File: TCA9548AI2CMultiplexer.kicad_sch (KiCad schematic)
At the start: 13 parts, among them U2 TCA9548APWR, U3 PCF8574TS

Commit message: Initial commit.
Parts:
- removed R41: 10kΩ, Resistor_SMD:R_0805_2012Metric, symbol Device:R
- removed R41 (x2): 0Ω, Resistor_SMD:R_0805_2012Metric, symbol Device:R
- added J14: ~{RESET}, Connector_PinHeader_2.54mm:PinHeader_1x02_P2.54mm_Vertical, symbol Connector_Generic:Conn_01x02
- added R32: 10kΩ, Resistor_SMD:R_0805_2012Metric, symbol Device:R
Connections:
- net +3.3V is gone; now on net +5V: C36.1, U2.24 (VCC)
- net +5V: now also C36.1, R32.1, R33.1, R35.1, U3.5 (VDD), R32.1
- net GND: now also J14.1 (Pin_1)
- net ~{RESET}I2C: no longer names the net of U2.3 (~{RESET})
- net ~{RESET}I2C: now also J14.2 (Pin_2), R32.2

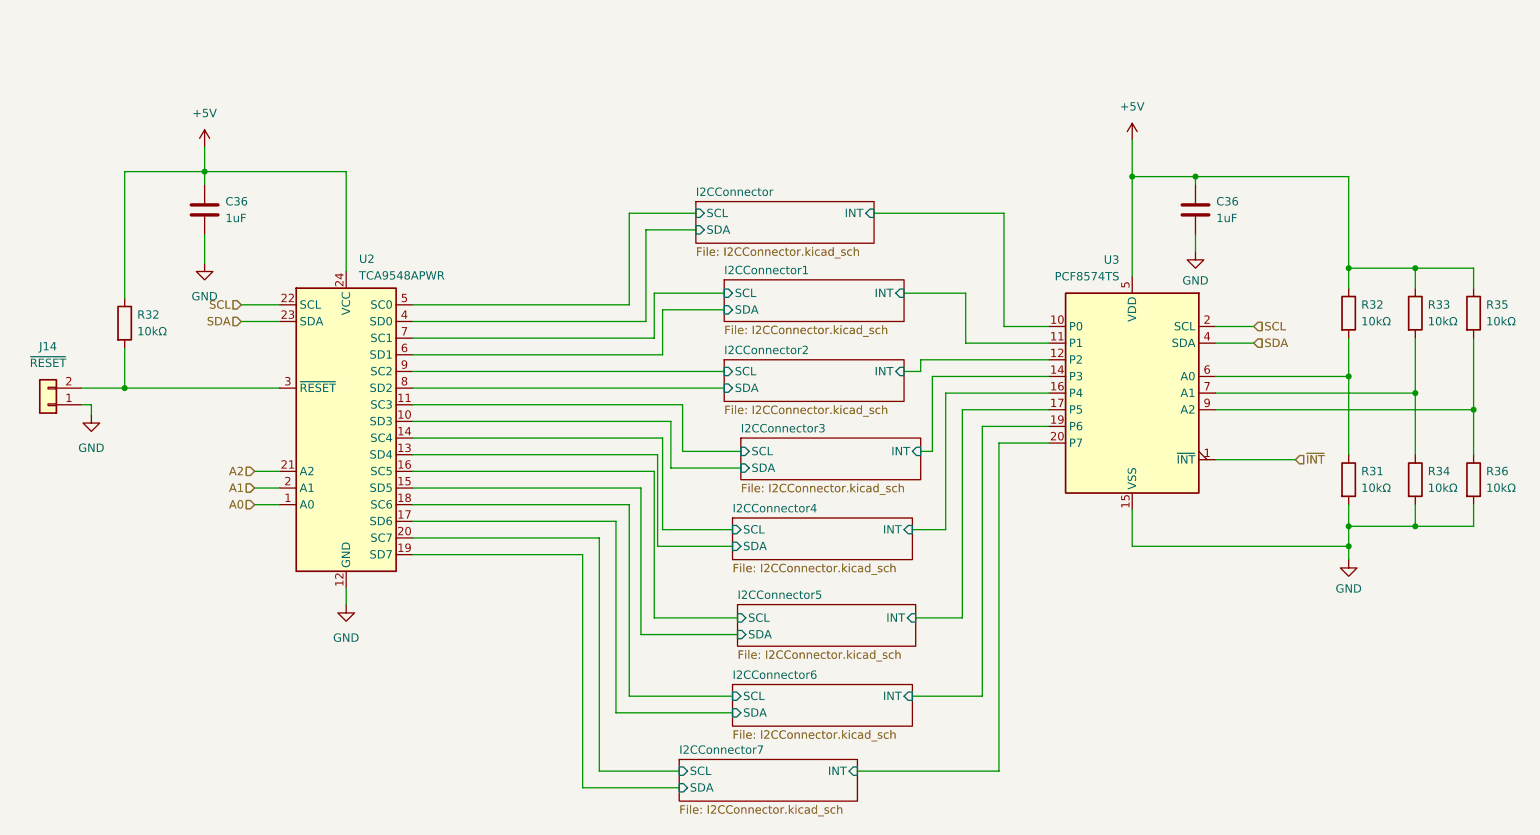
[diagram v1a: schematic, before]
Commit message: Swap I2C connections.
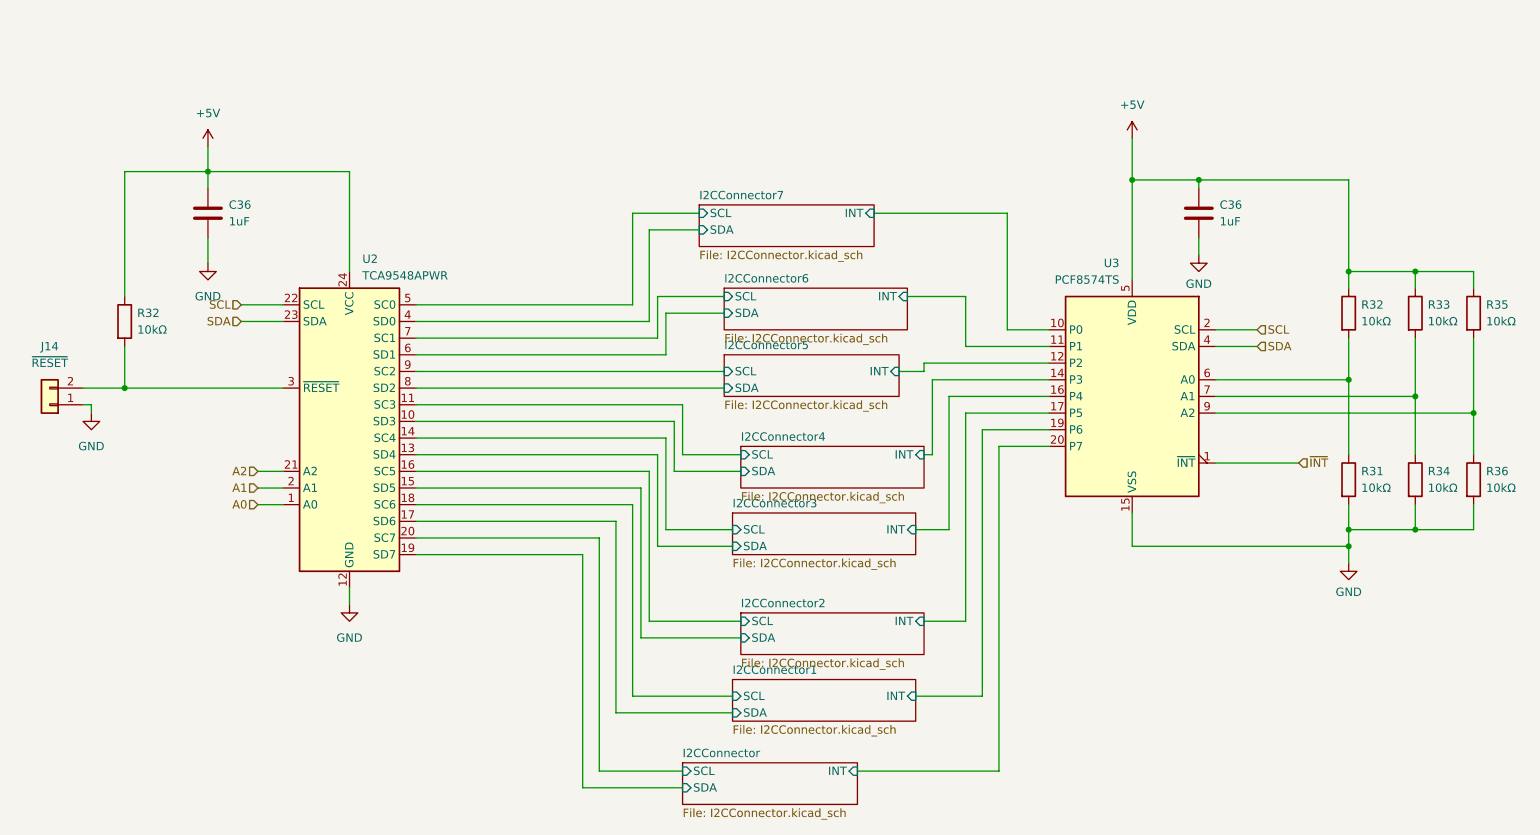
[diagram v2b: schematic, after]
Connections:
- net I2CConnector/INT: now also U3.20 (P7); no longer U3.10 (P0)
- net I2CConnector/SCL: now also U2.20 (SC7); no longer U2.5 (SC0)
- net I2CConnector/SDA: now also U2.19 (SD7); no longer U2.4 (SD0)
- net I2CConnector1/INT: now also U3.19 (P6); no longer U3.11 (P1)
- net I2CConnector1/SCL: now also U2.18 (SC6); no longer U2.7 (SC1)
- net I2CConnector1/SDA: now also U2.17 (SD6); no longer U2.6 (SD1)
- net I2CConnector2/INT: now also U3.17 (P5); no longer U3.12 (P2)
- net I2CConnector2/SCL: now also U2.16 (SC5); no longer U2.9 (SC2)
- net I2CConnector2/SDA: now also U2.15 (SD5); no longer U2.8 (SD2)
- net I2CConnector3/INT: now also U3.16 (P4); no longer U3.14 (P3)
- net I2CConnector3/SCL: now also U2.14 (SC4); no longer U2.11 (SC3)
- net I2CConnector3/SDA: now also U2.13 (SD4); no longer U2.10 (SD3)
- net I2CConnector4/INT: now also U3.14 (P3); no longer U3.16 (P4)
- net I2CConnector4/SCL: now also U2.11 (SC3); no longer U2.14 (SC4)
- net I2CConnector4/SDA: now also U2.10 (SD3); no longer U2.13 (SD4)
- net I2CConnector5/INT: now also U3.12 (P2); no longer U3.17 (P5)
- net I2CConnector5/SCL: now also U2.9 (SC2); no longer U2.16 (SC5)
- net I2CConnector5/SDA: now also U2.8 (SD2); no longer U2.15 (SD5)
- net I2CConnector6/INT: now also U3.11 (P1); no longer U3.19 (P6)
- net I2CConnector6/SCL: now also U2.7 (SC1); no longer U2.18 (SC6)
- net I2CConnector6/SDA: now also U2.6 (SD1); no longer U2.17 (SD6)
- net I2CConnector7/INT: now also U3.10 (P0); no longer U3.20 (P7)
- net I2CConnector7/SCL: now also U2.5 (SC0); no longer U2.20 (SC7)
- net I2CConnector7/SDA: now also U2.4 (SD0); no longer U2.19 (SD7)
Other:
- moved on the sheet: C36, U2, U3
